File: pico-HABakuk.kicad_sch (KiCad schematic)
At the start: 61 parts, among them J1 USB_B_Micro, J2 Ant+, J4 Ant-, J5 Solar, J7 Super_Cap, SW1 USB BOOT, SW2 RESET, U1 NCP1117-3.3_SOT223, U2 W25Q128JVS, U3 RP2040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

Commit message: More work on schematics and PCB
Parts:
- added C25: 220uF, Capacitor_Tantalum_SMD:CP_EIA-3216-10_Kemet-I, symbol Device:C_Polarized
- added D3: BAT54W, Package_TO_SOT_SMD:SOT-323_SC-70, symbol Diode:BAT54W
- added J3: GPS Ant, Connector_PinSocket_2.54mm:PinSocket_1x02_P2.54mm_Vertical, symbol Connector:Conn_01x02_Pin
- added J6: Debug, Connector_PinHeader_2.54mm:PinHeader_1x03_P2.54mm_Vertical, symbol Connector:Conn_01x03_Pin
- added JP2: GPS+Glonass, Jumper:SolderJumper-2_P1.3mm_Bridged_RoundedPad1.0x1.5mm, symbol Jumper:SolderJumper_2_Bridged
- added Q1: BSS84, Package_TO_SOT_SMD:SOT-23, symbol Transistor_FET:BSS84
- added R13: 100, Resistor_SMD:R_0603_1608Metric, symbol Device:R
- added R14: 2k7, Resistor_SMD:R_0603_1608Metric, symbol Device:R
- added R15: 3k9, Resistor_SMD:R_0603_1608Metric, symbol Device:R
- added R2: 10k, Resistor_SMD:R_0603_1608Metric, symbol Device:R
- added TP10: USB_D+, TestPoint:TestPoint_Pad_D1.5mm, symbol Connector:TestPoint
- added TP11: USB_D-, TestPoint:TestPoint_Pad_D1.5mm, symbol Connector:TestPoint
- added TP12: GND, TestPoint:TestPoint_Pad_D1.5mm, symbol Connector:TestPoint
- added TP13: USB_BOOT, TestPoint:TestPoint_Pad_D1.5mm, symbol Connector:TestPoint
- added TP14: Reset, TestPoint:TestPoint_Pad_D1.5mm, symbol Connector:TestPoint
- added TP15: SWCLK, TestPoint:TestPoint_Pad_D1.5mm, symbol Connector:TestPoint
- added TP16: SWD, TestPoint:TestPoint_Pad_D1.5mm, symbol Connector:TestPoint
- added TP9: +3V3, TestPoint:TestPoint_Pad_D1.5mm, symbol Connector:TestPoint
- C10, C11, C12, C13, C14, C15, C16, C2, C3, C5, C6, C7, C8, C9: footprint Capacitor_SMD:C_0402_1005Metric -> Capacitor_SMD:C_0603_1608Metric
- R1, R3, R4, R5: footprint Resistor_SMD:R_0402_1005Metric -> Resistor_SMD:R_0603_1608Metric
- R12: footprint (none) -> Resistor_SMD:R_0603_1608Metric
- TP1, TP2, TP3, TP4, TP5, TP6, TP7, TP8: footprint Connector_Pin:Pin_D1.1mm_L8.5mm_W2.5mm_FlatFork -> Connector_Pin:Pin_D1.1mm_L10.2mm_W3.5mm_Flat
- U6: value MAX-8Q -> GP-02
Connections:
- net +3V3: now also D3.1 (A), Q1.3 (D), R14.1, R2.2, TP9.1; no longer U6.8 (VCC)
- net GND: now also C25.2, J3.2 (Pin_2), J6.2 (Pin_2), JP2.1 (A), R15.2, TP12.1
- net GPIO5: now also R13.2
- net RUN: now also R14.2, R15.1, TP14.1
- net SWCLK: now also J6.1 (Pin_1), TP15.1
- net SWD: now also J6.3 (Pin_3), TP16.1
- net USB_D+: now also TP10.1
- net USB_D-: now also TP11.1
- net ~{USB_BOOT}: now also TP13.1
- net at U6.11 (RF_IN): now also J3.1 (Pin_1)
- net at U6.13 (LNA_EN): now also JP2.2 (B)
- net at U6.6 (V_BCKP): now also C25.1, D3.3 (K)
- new net: Q1.1 (G), R13.1, R2.1
- new net: Q1.2 (S), U6.8 (VCC)
- no-connect marks 2 -> 10
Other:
- moved on the sheet: R1, TP2, TP3, TP4, TP5, TP6, TP7, TP8

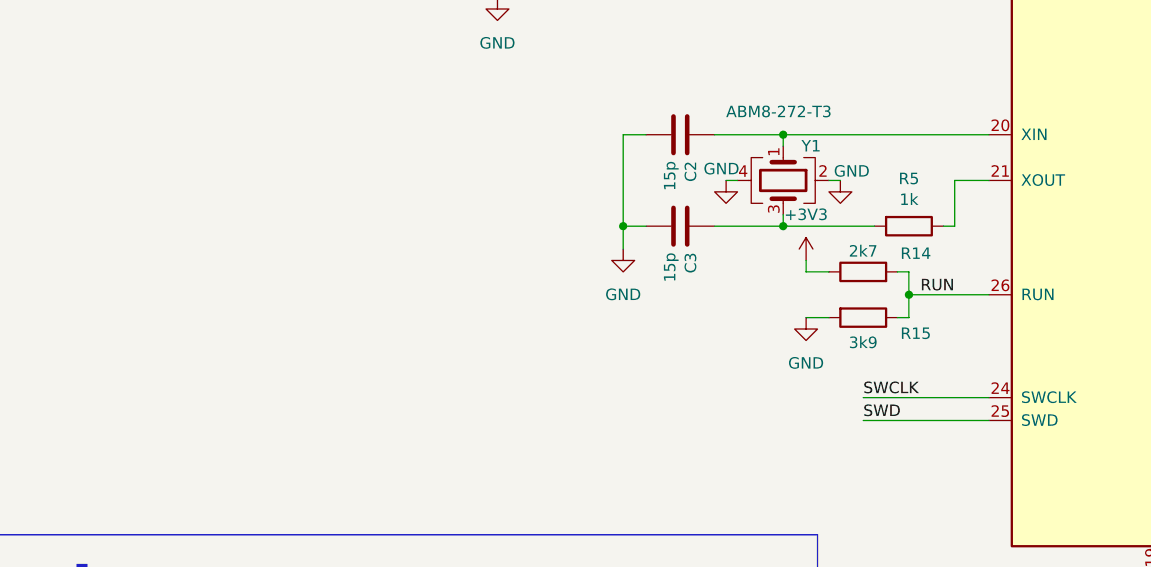
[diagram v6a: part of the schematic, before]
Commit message: Max809 added
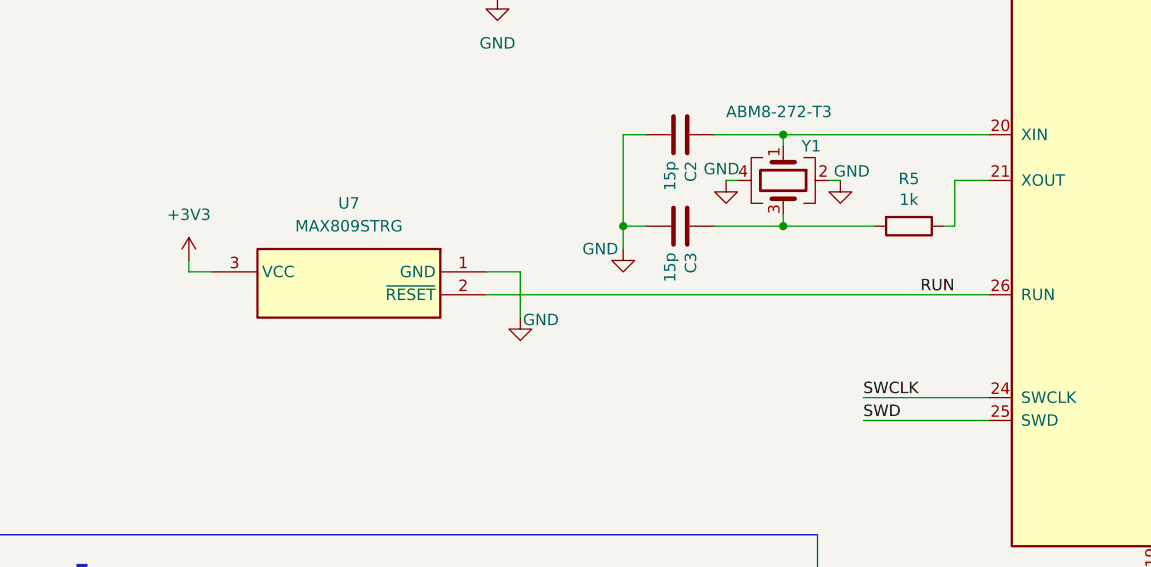
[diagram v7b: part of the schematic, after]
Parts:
- removed R14: 2k7, Resistor_SMD:R_0603_1608Metric, symbol Device:R
- removed R15: 3k9, Resistor_SMD:R_0603_1608Metric, symbol Device:R
- added U7: MAX809STRG, SOT65P210X110-3N, symbol MAX809:MAX809SEXR+T
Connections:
- net +3V3: now also U7.3 (VCC)
- net GND: now also U7.1 (GND)
- net RUN: now also U7.2 (~{RESET})

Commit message: Work on PCB
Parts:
- D1: footprint _moje_footprints:STMITE -> SamacSys_Parts:SMM4F15ATR
- U7: footprint SOT65P210X110-3N -> SamacSys_Parts:SOT65P210X110-3N
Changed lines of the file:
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@@
 			)
 		)
-		(property "Footprint" "_moje_footprints:STMITE"
+		(property "Footprint" "SamacSys_Parts:SMM4F15ATR"
 			(at 137.16 55.88 0)
 			(effects
@@
 			)
 		)
-		(property "Footprint" "SOT65P210X110-3N"
+		(property "Footprint" "SamacSys_Parts:SOT65P210X110-3N"
 			(at 83.82 257.48 0)
 			(effects
